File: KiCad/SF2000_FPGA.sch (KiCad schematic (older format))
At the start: 7 parts, among them J3 Conn_02x03_Odd_Even, J4 Conn_02x01, U7 10M04SCE144

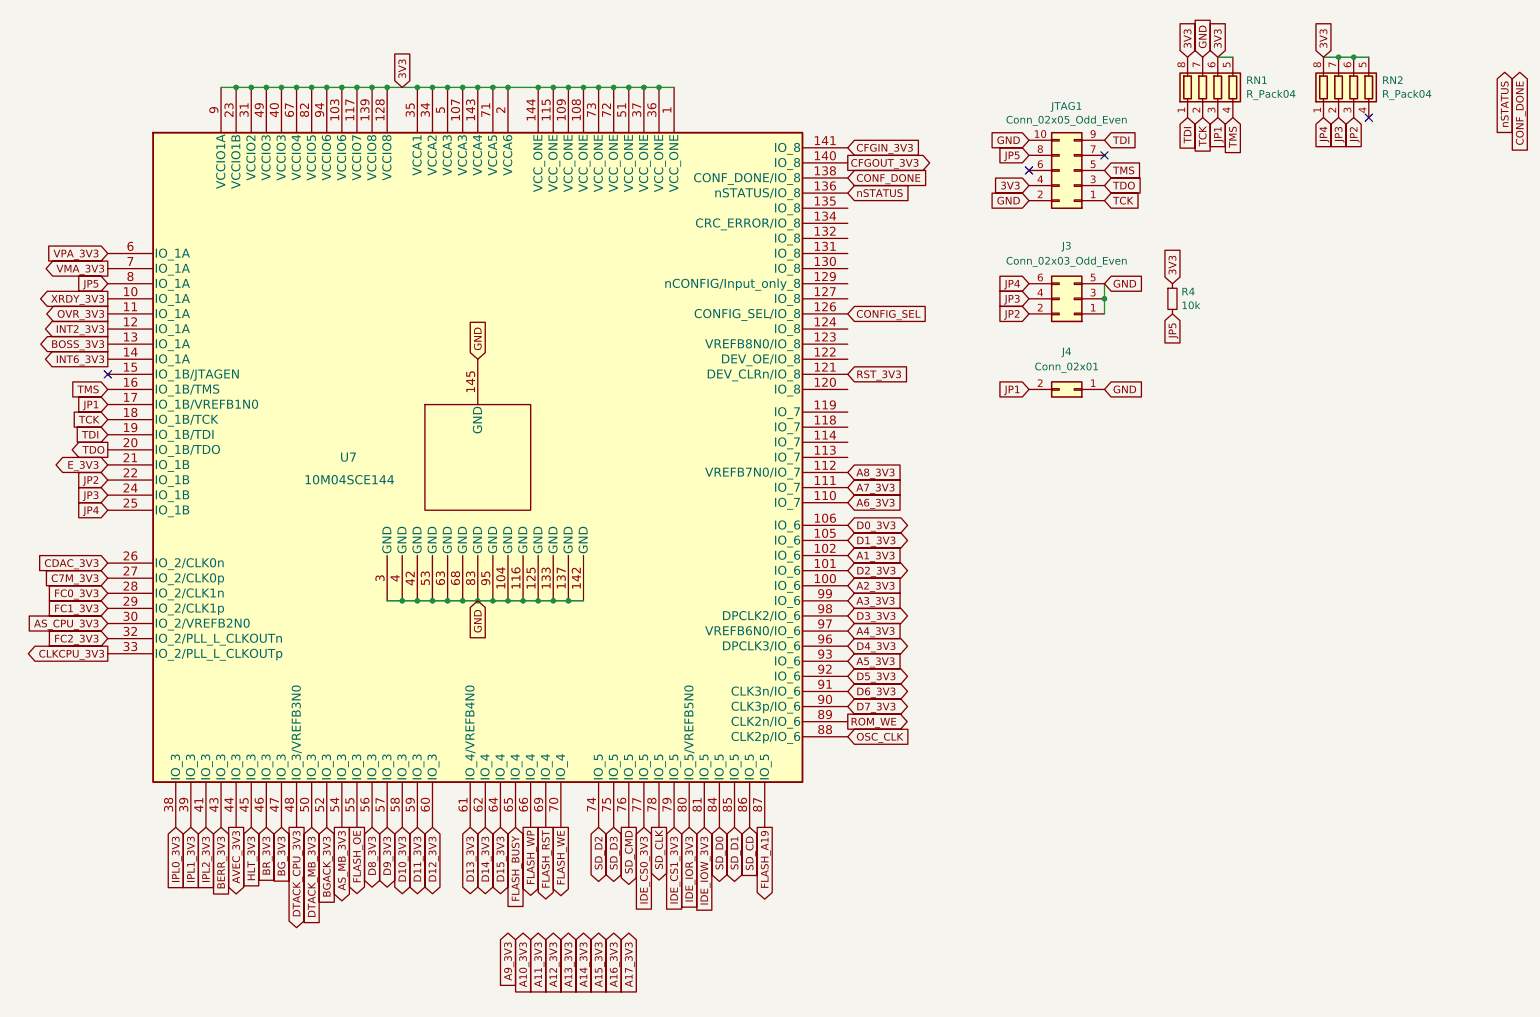
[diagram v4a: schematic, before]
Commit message: more routing and fixing of FPGA pin assignments
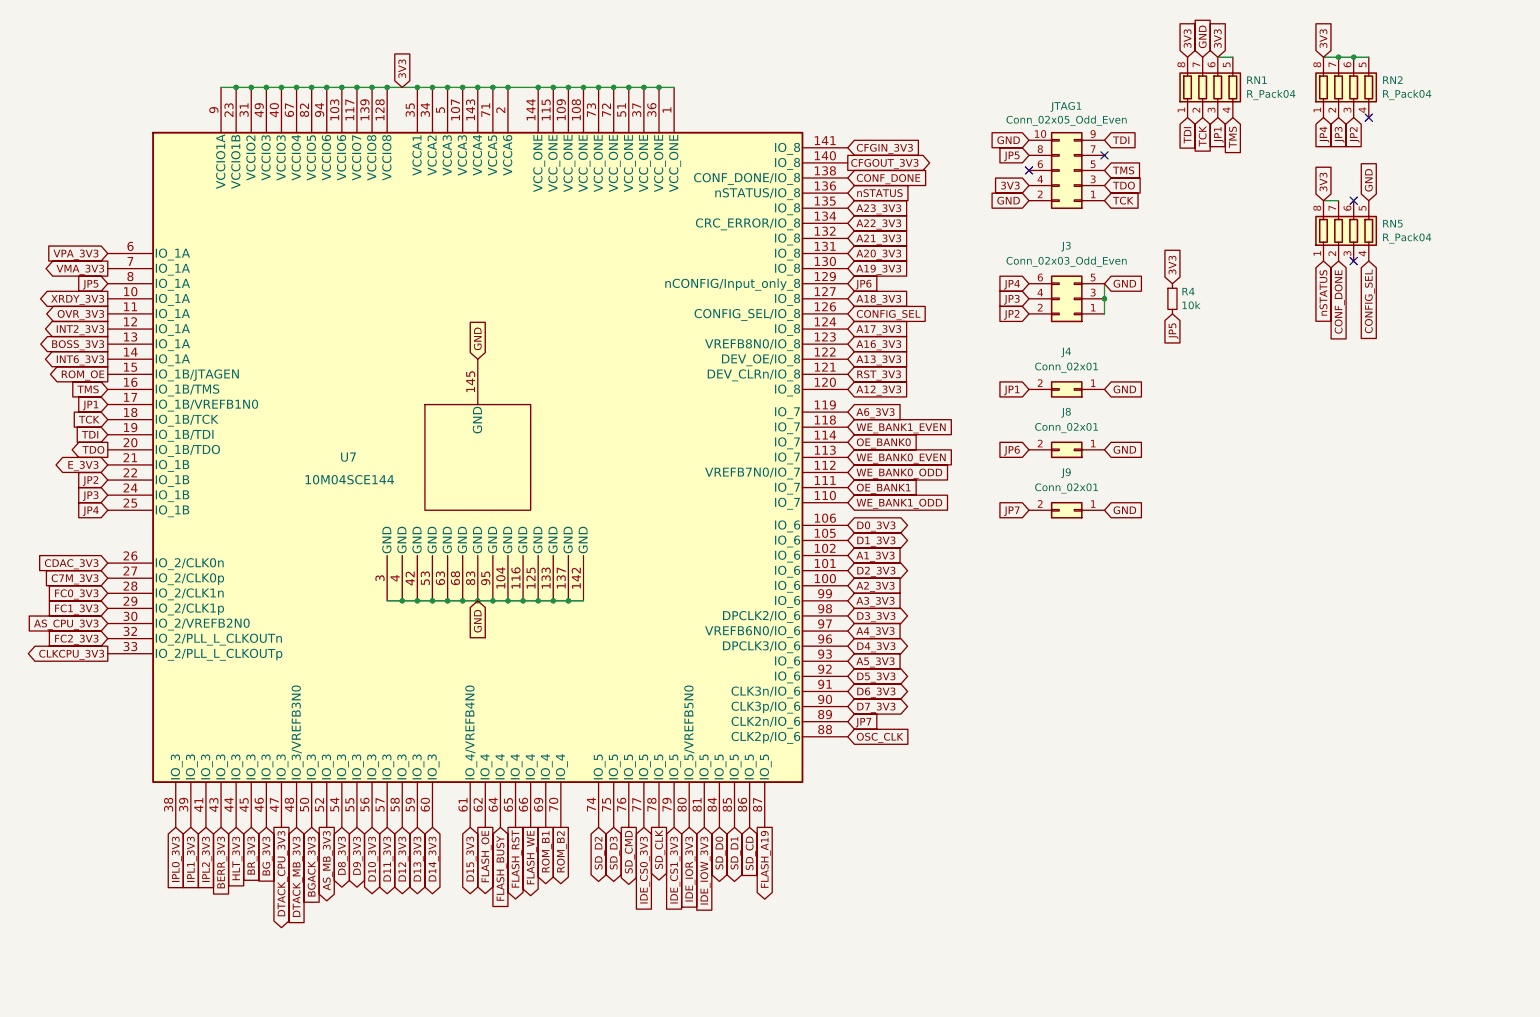
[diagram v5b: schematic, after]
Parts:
- added J8, J9: Conn_02x01, Connector_PinHeader_2.00mm:PinHeader_2x01_P2.00mm_Vertical, symbol Connector_Generic:Conn_02x01
- added RN5: R_Pack04, SF2000:RESCAF80P320X160X60-8N, symbol Device:R_Pack04
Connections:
- net AVEC_3V3 is gone; now on net HLT_3V3: U7.44 (IO_3)
- net FLASH_WP is gone; now on net FLASH_WE: U7.66 (IO_4)
- net 3V3: now also RN5.7 (R2.2), RN5.8 (R1.2)
- net A12_3V3: now also U7.120 (IO_8)
- net A13_3V3: now also U7.122 (DEV_OE/IO_8)
- net A16_3V3: now also U7.123 (VREFB8N0/IO_8)
- net A17_3V3: now also U7.124 (IO_8)
- net A6_3V3: now also U7.119 (IO_7); no longer U7.110 (IO_7)
- net AS_MB_3V3: now also U7.52 (IO_3); no longer U7.54 (IO_3)
- net BGACK_3V3: now also U7.50 (IO_3); no longer U7.52 (IO_3)
- net BG_3V3: now also U7.46 (IO_3); no longer U7.47 (IO_3)
- net BR_3V3: now also U7.45 (IO_3); no longer U7.46 (IO_3)
- net CONFIG_SEL: now also RN5.4 (R4.1)
- net CONF_DONE: now also RN5.2 (R2.1)
- net D10_3V3: now also U7.56 (IO_3); no longer U7.58 (IO_3)
- net D11_3V3: now also U7.57 (IO_3); no longer U7.59 (IO_3)
- net D12_3V3: now also U7.58 (IO_3); no longer U7.60 (IO_3)
- net D13_3V3: now also U7.59 (IO_3); no longer U7.61 (IO_4/VREFB4N0)
- net D14_3V3: now also U7.60 (IO_3); no longer U7.62 (IO_4)
- net D15_3V3: now also U7.61 (IO_4/VREFB4N0); no longer U7.64 (IO_4)
- net D8_3V3: now also U7.54 (IO_3); no longer U7.56 (IO_3)
- net D9_3V3: now also U7.55 (IO_3); no longer U7.57 (IO_3)
- net DTACK_CPU_3V3: now also U7.47 (IO_3); no longer U7.48 (IO_3/VREFB3N0)
- net DTACK_MB_3V3: now also U7.48 (IO_3/VREFB3N0); no longer U7.50 (IO_3)
- net FLASH_BUSY: now also U7.64 (IO_4); no longer U7.65 (IO_4)
- net FLASH_OE: now also U7.62 (IO_4); no longer U7.55 (IO_3)
- net FLASH_RST: now also U7.65 (IO_4); no longer U7.69 (IO_4)
- net FLASH_WE: no longer U7.70 (IO_4)
- net GND: now also J8.1 (Pin_1), J9.1 (Pin_1), RN5.5 (R4.2)
- net HLT_3V3: no longer U7.45 (IO_3)
- net nSTATUS: now also RN5.1 (R1.1)
- net WE_BANK0_EVEN: now reaches U7.113 (IO_7)
- net OE_BANK0: now reaches U7.114 (IO_7)
- net WE_BANK1_EVEN: now reaches U7.118 (IO_7)
- net A18_3V3: now reaches U7.127 (IO_8)
- net JP6: now reaches U7.129 (nCONFIG/Input_only_8)
- net JP6: now also J8.2 (Pin_2)
- net A19_3V3: now reaches U7.130 (IO_8)
- net A20_3V3: now reaches U7.131 (IO_8)
- net A21_3V3: now reaches U7.132 (IO_8)
- net A22_3V3: now reaches U7.134 (CRC_ERROR/IO_8)
- net A23_3V3: now reaches U7.135 (IO_8)
- net ROM_OE: now reaches U7.15 (IO_1B/JTAGEN)
- net A7_3V3 renamed OE_BANK1
- net A8_3V3 renamed WE_BANK0_ODD
- net ROM_WE renamed JP7
- net JP7: now also J9.2 (Pin_2)
- new net ROM_B1: U7.69 (IO_4)
- new net ROM_B2: U7.70 (IO_4)
- new net WE_BANK1_ODD: U7.110 (IO_7)
- no-connect marks 4 -> 5
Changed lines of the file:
@@
 Text GLabel 1350 4750 0    50   Input ~ 0
 FC2_3V3
-Text GLabel 4200 6700 3    50   Input ~ 0
-A11_3V3
-Text GLabel 4000 6700 3    50   Input ~ 0
-A9_3V3
-Text GLabel 4100 6700 3    50   Input ~ 0
-A10_3V3
-Text GLabel 4300 6700 3    50   Input ~ 0
+Text GLabel 6250 2200 2    50   Input ~ 0
+A20_3V3
+Text GLabel 6250 2000 2    50   Input ~ 0
+A22_3V3
+Text GLabel 6250 2100 2    50   Input ~ 0
+A21_3V3
+Text GLabel 6250 3100 2    50   Input ~ 0
 A12_3V3
 Text GLabel 1800 6000 3    50   Input ~ 0
@@
 Text GLabel 2100 6000 3    50   Input ~ 0
 BERR_3V3
-Text GLabel 4400 6700 3    50   Input ~ 0
+Text GLabel 6250 2900 2    50   Input ~ 0
 A13_3V3
-Text GLabel 4500 6700 3    50   Input ~ 0
-A14_3V3
-Text GLabel 4600 6700 3    50   Input ~ 0
-A15_3V3
-Text GLabel 4700 6700 3    50   Input ~ 0
+Text GLabel 6250 2500 2    50   Input ~ 0
+A18_3V3
+Text GLabel 6250 2300 2    50   Input ~ 0
+A19_3V3
+Text GLabel 6250 2800 2    50   Input ~ 0
 A16_3V3
-Text GLabel 4800 6700 3    50   Input ~ 0
+Text GLabel 6250 2700 2    50   Input ~ 0
 A17_3V3
 Text GLabel 1350 2200 0    50   Input ~ 0
@@
 Text GLabel 1350 4650 0    50   Input ~ 0
 AS_CPU_3V3
-NoConn ~ 1350 3000
 Text GLabel 6250 1500 2    50   Input ~ 0
 CFGIN_3V3
 Text GLabel 6250 1600 2    50   Output ~ 0
 CFGOUT_3V3
-Text GLabel 2200 6000 3    50   Output ~ 0
-AVEC_3V3
 Text GLabel 6250 3000 2    50   Input ~ 0
 RST_3V3
+Text GLabel 2200 6000 3    50   Input ~ 0
+HLT_3V3
 Text GLabel 2300 6000 3    50   Input ~ 0
-HLT_3V3
+BR_3V3
 Text GLabel 2400 6000 3    50   Input ~ 0
-BR_3V3
-Text GLabel 2500 6000 3    50   Input ~ 0
 BG_3V3
-Text GLabel 2600 6000 3    50   Output ~ 0
+Text GLabel 2500 6000 3    50   Output ~ 0
 DTACK_CPU_3V3
+Text GLabel 2600 6000 3    50   Input ~ 0
+DTACK_MB_3V3
 Text GLabel 2700 6000 3    50   Input ~ 0
-DTACK_MB_3V3
-Text GLabel 2800 6000 3    50   Input ~ 0
 BGACK_3V3
-Text GLabel 2900 6000 3    50   Output ~ 0
+Text GLabel 2800 6000 3    50   Output ~ 0
 AS_MB_3V3
 $Comp
@@
 Wire Wire Line
 	9600 900  9700 900
-Text GLabel 10600 1000 3    50   Input ~ 0
+Text GLabel 9400 2250 3    50   Input ~ 0
 nSTATUS
-Text GLabel 10700 1000 3    50   Input ~ 0
+Text GLabel 9500 2250 3    50   Input ~ 0
 CONF_DONE
 Text GLabel 9400 1300 3    50   Input ~ 0
@@
 Text GLabel 1350 2300 0    50   Output ~ 0
 VMA_3V3
+Text GLabel 3000 6000 3    50   BiDi ~ 0
+D9_3V3
+Text GLabel 3100 6000 3    50   BiDi ~ 0
+D10_3V3
 Text GLabel 3200 6000 3    50   BiDi ~ 0
-D9_3V3
+D11_3V3
 Text GLabel 3300 6000 3    50   BiDi ~ 0
-D10_3V3
+D12_3V3
 Text GLabel 3400 6000 3    50   BiDi ~ 0
-D11_3V3
+D13_3V3
 Text GLabel 3500 6000 3    50   BiDi ~ 0
-D12_3V3
+D14_3V3
 Text GLabel 3750 6000 3    50   BiDi ~ 0
-D13_3V3
-Text GLabel 3850 6000 3    50   BiDi ~ 0
-D14_3V3
-Text GLabel 3950 6000 3    50   BiDi ~ 0
 D15_3V3
-Text GLabel 3100 6000 3    50   BiDi ~ 0
+Text GLabel 2900 6000 3    50   BiDi ~ 0
 D8_3V3
-Text GLabel 3000 6000 3    50   Output ~ 0
-FLASH_OE
-Text GLabel 4350 6000 3    50   Output ~ 0
+Text GLabel 4150 6000 3    50   Output ~ 0
 FLASH_WE
-Text GLabel 4250 6000 3    50   Output ~ 0
+Text GLabel 4050 6000 3    50   Output ~ 0
 FLASH_RST
-Text GLabel 4150 6000 3    50   Output ~ 0
-FLASH_WP
-Text GLabel 4050 6000 3    50   Input ~ 0
+Text GLabel 3950 6000 3    50   Input ~ 0
 FLASH_BUSY
 Text GLabel 5400 6000 3    50   BiDi ~ 0
@@
 Text GLabel 6250 4900 2    50   Input ~ 0
 A5_3V3
-Text GLabel 6250 3850 2    50   Input ~ 0
+Text GLabel 6250 3250 2    50   Input ~ 0
 A6_3V3
 Text GLabel 6250 4700 2    50   Input ~ 0
@@
 Text GLabel 6250 4500 2    50   Input ~ 0
 A3_3V3
-Text GLabel 6250 3750 2    50   Input ~ 0
-A7_3V3
-Text GLabel 6250 3650 2    50   Input ~ 0
-A8_3V3
+Text GLabel 6250 1900 2    50   Input ~ 0
+A23_3V3
 Text GLabel 6250 4400 2    50   Input ~ 0
 A2_3V3
@@
 Text GLabel 6250 5400 2    50   Input ~ 0
 OSC_CLK
-Text GLabel 6250 5300 2    50   Output ~ 0
-ROM_WE
+Text GLabel 6250 3750 2    50   Input ~ 0
+OE_BANK1
+Text GLabel 6250 3350 2    50   Input ~ 0
+WE_BANK1_EVEN
+Text GLabel 6250 3850 2    50   Input ~ 0
+WE_BANK1_ODD
+Text GLabel 6250 3450 2    50   Input ~ 0
+OE_BANK0
+Text GLabel 6250 3550 2    50   Input ~ 0
+WE_BANK0_EVEN
+Text GLabel 6250 3650 2    50   Input ~ 0
+WE_BANK0_ODD
+$Comp
+L Device:R_Pack04 RN5
+U 1 1 62107318
+P 9600 2050
+F 0 "RN5" H 9788 2096 50  0000 L CNN
+F 1 "R_Pack04" H 9788 2005 50  0000 L CNN
+F 2 "SF2000:RESCAF80P320X160X60-8N" V 9875 2050 50  0001 C CNN
+F 3 "~" H 9600 2050 50  0001 C CNN
+	1    9600 2050
+	1    0    0    -1
+$EndComp
+Text GLabel 9700 2250 3    50   Input ~ 0
+CONFIG_SEL
+NoConn ~ 9600 1850
+NoConn ~ 9600 2250
+Text GLabel 9400 1850 1    50   Input ~ 0
+3V3
+Wire Wire Line
+	9400 1850 9500 1850
+Text GLabel 9700 1850 1    50   Input ~ 0
+GND
+Text GLabel 6250 2400 2    50   Input ~ 0
+JP6
+$Comp
+L Connector_Generic:Conn_02x01 J8
+U 1 1 62127717
+P 7750 3500
+F 0 "J8" H 7800 3250 50  0000 C CNN
+F 1 "Conn_02x01" H 7800 3350 50  0000 C CNN
+F 2 "Connector_PinHeader_2.00mm:PinHeader_2x01_P2.00mm_Vertical" H 7750 3500 50  0001 C CNN
+F 3 "~" H 7750 3500 50  0001 C CNN
+	1    7750 3500
+	-1   0    0    1
+$EndComp
+Text GLabel 7950 3500 2    50   Input ~ 0
+GND
+Text GLabel 7450 3500 0    50   Input ~ 0
+JP6
+$Comp
+L Connector_Generic:Conn_02x01 J9
+U 1 1 62132436
+P 7750 3900
+F 0 "J9" H 7800 3650 50  0000 C CNN
+F 1 "Conn_02x01" H 7800 3750 50  0000 C CNN
+F 2 "Connector_PinHeader_2.00mm:PinHeader_2x01_P2.00mm_Vertical" H 7750 3900 50  0001 C CNN
+F 3 "~" H 7750 3900 50  0001 C CNN
+	1    7750 3900
+	-1   0    0    1
+$EndComp
+Text GLabel 7950 3900 2    50   Input ~ 0
+GND
+Text GLabel 7450 3900 0    50   Input ~ 0
+JP7
+Text GLabel 6250 5300 2    50   Input ~ 0
+JP7
+Text GLabel 3850 6000 3    50   Output ~ 0
+FLASH_OE
+Text GLabel 1350 3000 0    50   Output ~ 0
+ROM_OE
+Text GLabel 4250 6000 3    50   Output ~ 0
+ROM_B1
+Text GLabel 4350 6000 3    50   Output ~ 0
+ROM_B2
 $EndSCHEMATC

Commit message: more routing and fixed pull-up resistors for Flash mem control signals
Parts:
- renumbered RN5 to RN6
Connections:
- net BERR_3V3 is gone; now on net BG_3V3: U7.43 (IO_3)
- net IPL1_3V3 is gone; now on net HLT_3V3: U7.39 (IO_3)
- net IPL2_3V3 is gone; now on net BR_3V3: U7.41 (IO_3)
- net AS_MB_3V3: now also U7.48 (IO_3/VREFB3N0); no longer U7.52 (IO_3)
- net BGACK_3V3: now also U7.47 (IO_3); no longer U7.50 (IO_3)
- net BG_3V3: no longer U7.46 (IO_3)
- net BR_3V3: no longer U7.45 (IO_3)
- net D10_3V3: now also U7.54 (IO_3); no longer U7.56 (IO_3)
- net D11_3V3: now also U7.55 (IO_3); no longer U7.57 (IO_3)
- net D12_3V3: now also U7.56 (IO_3); no longer U7.58 (IO_3)
- net D13_3V3: now also U7.57 (IO_3); no longer U7.59 (IO_3)
- net D14_3V3: now also U7.58 (IO_3); no longer U7.60 (IO_3)
- net D15_3V3: now also U7.59 (IO_3); no longer U7.61 (IO_4/VREFB4N0)
- net D8_3V3: now also U7.50 (IO_3); no longer U7.54 (IO_3)
- net D9_3V3: now also U7.52 (IO_3); no longer U7.55 (IO_3)
- net DTACK_CPU_3V3: now also U7.44 (IO_3); no longer U7.47 (IO_3)
- net DTACK_MB_3V3: now also U7.46 (IO_3); no longer U7.48 (IO_3/VREFB3N0)
- net FLASH_OE: now also U7.60 (IO_3); no longer U7.62 (IO_4)
- net HLT_3V3: no longer U7.44 (IO_3)
- net IPL0_3V3 renamed AVEC_3V3
- new net LDS_3V3: U7.61 (IO_4/VREFB4N0)
- new net RW_3V3: U7.45 (IO_3)
- new net UDS_3V3: U7.62 (IO_4)
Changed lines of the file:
@@
 Text GLabel 6250 3100 2    50   Input ~ 0
 A12_3V3
+Text GLabel 3850 6000 3    50   Input ~ 0
+UDS_3V3
+Text GLabel 3750 6000 3    50   Input ~ 0
+LDS_3V3
+Text GLabel 2300 6000 3    50   Input ~ 0
+RW_3V3
 Text GLabel 1800 6000 3    50   Input ~ 0
-IPL0_3V3
-Text GLabel 1900 6000 3    50   Input ~ 0
-IPL1_3V3
-Text GLabel 2000 6000 3    50   Input ~ 0
-IPL2_3V3
-Text GLabel 2100 6000 3    50   Input ~ 0
-BERR_3V3
+AVEC_3V3
 Text GLabel 6250 2900 2    50   Input ~ 0
 A13_3V3
@@
 Text GLabel 6250 3000 2    50   Input ~ 0
 RST_3V3
-Text GLabel 2200 6000 3    50   Input ~ 0
+Text GLabel 1900 6000 3    50   Input ~ 0
 HLT_3V3
-Text GLabel 2300 6000 3    50   Input ~ 0
+Text GLabel 2000 6000 3    50   Input ~ 0
 BR_3V3
+Text GLabel 2100 6000 3    50   Input ~ 0
+BG_3V3
+Text GLabel 2200 6000 3    50   Output ~ 0
+DTACK_CPU_3V3
 Text GLabel 2400 6000 3    50   Input ~ 0
-BG_3V3
-Text GLabel 2500 6000 3    50   Output ~ 0
-DTACK_CPU_3V3
-Text GLabel 2600 6000 3    50   Input ~ 0
 DTACK_MB_3V3
-Text GLabel 2700 6000 3    50   Input ~ 0
+Text GLabel 2500 6000 3    50   Input ~ 0
 BGACK_3V3
-Text GLabel 2800 6000 3    50   Output ~ 0
+Text GLabel 2600 6000 3    50   Output ~ 0
 AS_MB_3V3
 $Comp
@@
 Text GLabel 1350 2300 0    50   Output ~ 0
 VMA_3V3
+Text GLabel 2800 6000 3    50   BiDi ~ 0
+D9_3V3
+Text GLabel 2900 6000 3    50   BiDi ~ 0
+D10_3V3
 Text GLabel 3000 6000 3    50   BiDi ~ 0
-D9_3V3
+D11_3V3
 Text GLabel 3100 6000 3    50   BiDi ~ 0
-D10_3V3
+D12_3V3
 Text GLabel 3200 6000 3    50   BiDi ~ 0
-D11_3V3
+D13_3V3
 Text GLabel 3300 6000 3    50   BiDi ~ 0
-D12_3V3
+D14_3V3
 Text GLabel 3400 6000 3    50   BiDi ~ 0
-D13_3V3
-Text GLabel 3500 6000 3    50   BiDi ~ 0
-D14_3V3
-Text GLabel 3750 6000 3    50   BiDi ~ 0
 D15_3V3
-Text GLabel 2900 6000 3    50   BiDi ~ 0
+Text GLabel 2700 6000 3    50   BiDi ~ 0
 D8_3V3
 Text GLabel 4150 6000 3    50   Output ~ 0
@@
 WE_BANK0_ODD
 $Comp
-L Device:R_Pack04 RN5
+L Device:R_Pack04 RN6
 U 1 1 62107318
 P 9600 2050
-F 0 "RN5" H 9788 2096 50  0000 L CNN
+F 0 "RN6" H 9788 2096 50  0000 L CNN
 F 1 "R_Pack04" H 9788 2005 50  0000 L CNN
 F 2 "SF2000:RESCAF80P320X160X60-8N" V 9875 2050 50  0001 C CNN
@@
 Text GLabel 6250 5300 2    50   Input ~ 0
 JP7
-Text GLabel 3850 6000 3    50   Output ~ 0
+Text GLabel 3500 6000 3    50   Output ~ 0
 FLASH_OE
 Text GLabel 1350 3000 0    50   Output ~ 0

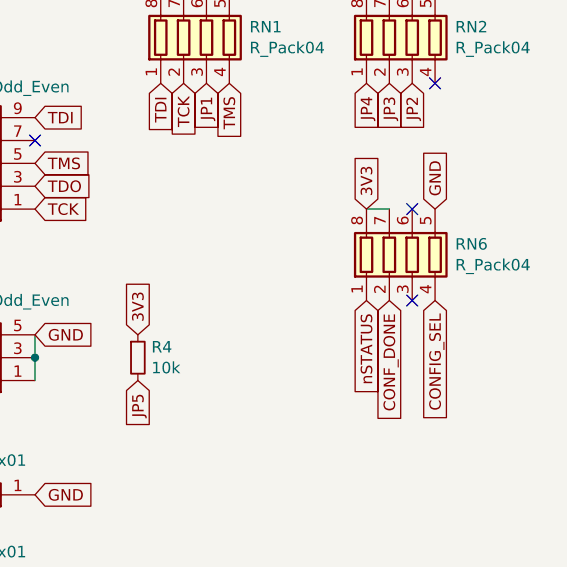
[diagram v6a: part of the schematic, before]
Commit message: more routing, fixed JP6 placement and RN6 + some silkscreen fixes
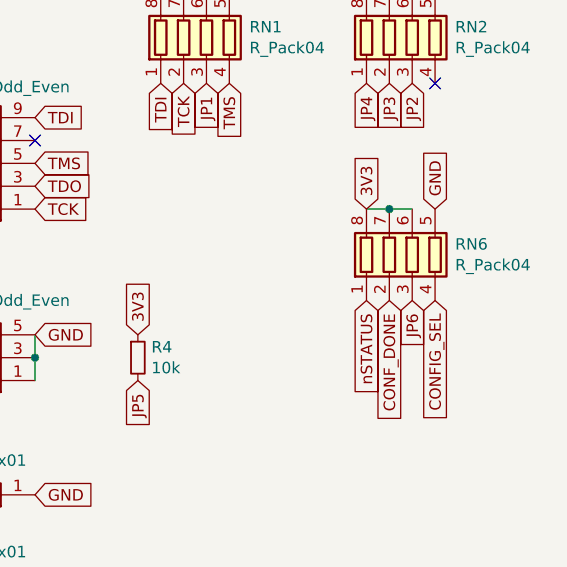
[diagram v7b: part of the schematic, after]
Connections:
- net 3V3: now also RN6.6 (R3.2)
- net JP6: now also RN6.3 (R3.1)
- no-connect marks 5 -> 3
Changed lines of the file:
@@
 Text GLabel 9700 2250 3    50   Input ~ 0
 CONFIG_SEL
-NoConn ~ 9600 1850
-NoConn ~ 9600 2250
 Text GLabel 9400 1850 1    50   Input ~ 0
 3V3
@@
 Text GLabel 4350 6000 3    50   Output ~ 0
 ROM_B2
+Wire Wire Line
+	9500 1850 9600 1850
+Connection ~ 9500 1850
+Text GLabel 9600 2250 3    50   Input ~ 0
+JP6
 $EndSCHEMATC
